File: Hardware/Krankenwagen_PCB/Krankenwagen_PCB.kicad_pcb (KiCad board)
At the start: 2 copper layers, 292.1 x 139 mm, 0 parts

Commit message: Basic PCB completed, added logos to silkscreen
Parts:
- added G***: LOGO, Combat_Robotics:Logo, B.Cu at (134.7, 78.9)
- added G***: LOGO, Combat_Robotics:Krankenwagen_Logo, B.Cu at (173.1, 126.7)
- added H1: 3.5mm Plated Holes, Combat_Robotics:Solder Holes MAMBA X Power, F.Cu at (148.6, 93.6)
- added H4: 2.8mm Plated Holes, Solder_Holes:2.8mm Solder Hole x3, F.Cu at (156.0, 71.9)
- added H7: 2.8mm Plated Holes, Solder_Holes:2.8mm Solder Hole x3, F.Cu at (181.0, 86.1)
- added J1: XT60-M, XT_Connectors:AMASS_XT60-F_1x02_P7.20mm_Vertical, F.Cu at (80.8, 82.6)
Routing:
- net Net-(H4-Pad1): track 0.00 -> 73.3 mm
- net Net-(H4-Pad2): track 0.00 -> 44.1 mm
- net Net-(H4-Pad3): track 0.00 -> 19.7 mm
- added copper zone on B.Cu, net +12V
- added copper zone on F.Cu, net +12V
- added copper zone on B.Cu, net GND
- added copper zone on F.Cu, net GND
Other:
- board size 292.1 x 139 mm -> 119.8 x 88.6 mm
- board text added: "+12V"
- board text added: "Castle 1410"
- board text added: "GND"
- board text added: "MAMBA X"

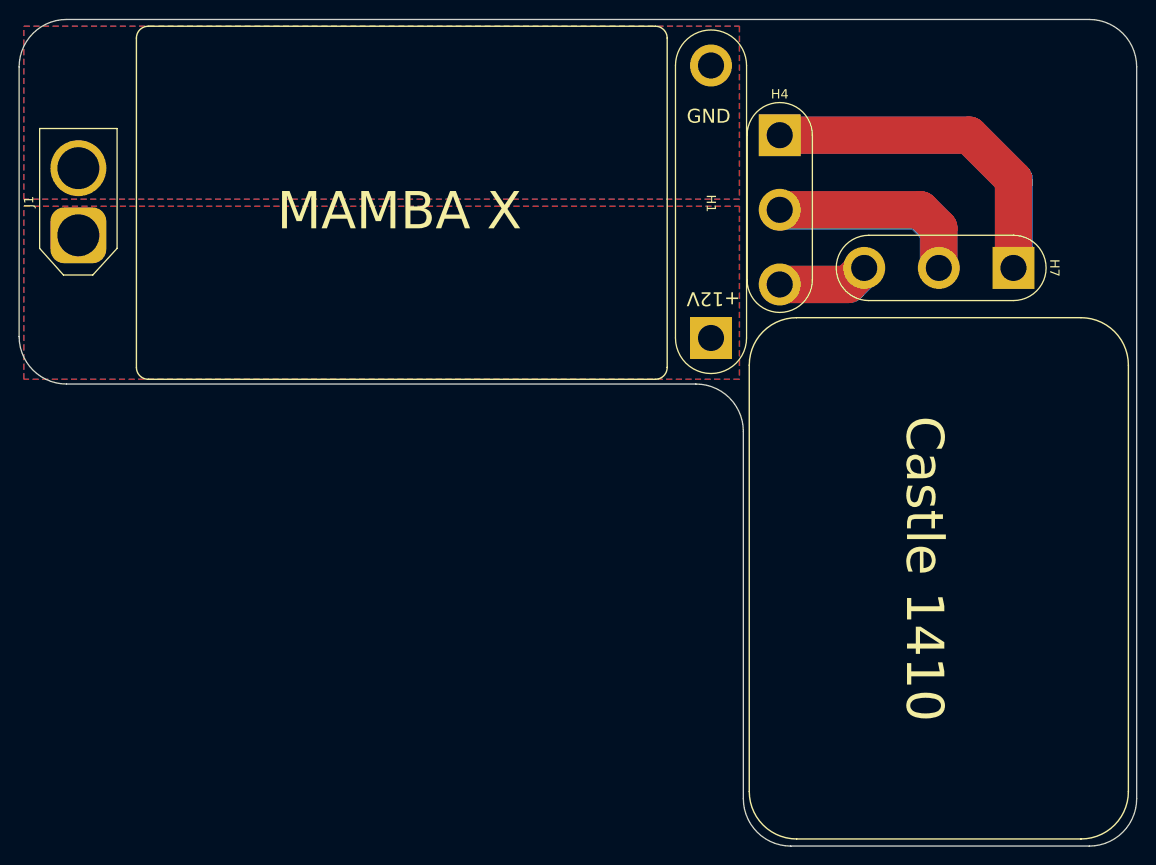
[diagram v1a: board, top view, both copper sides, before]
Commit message: Added mounting holes to PCB and Schematic
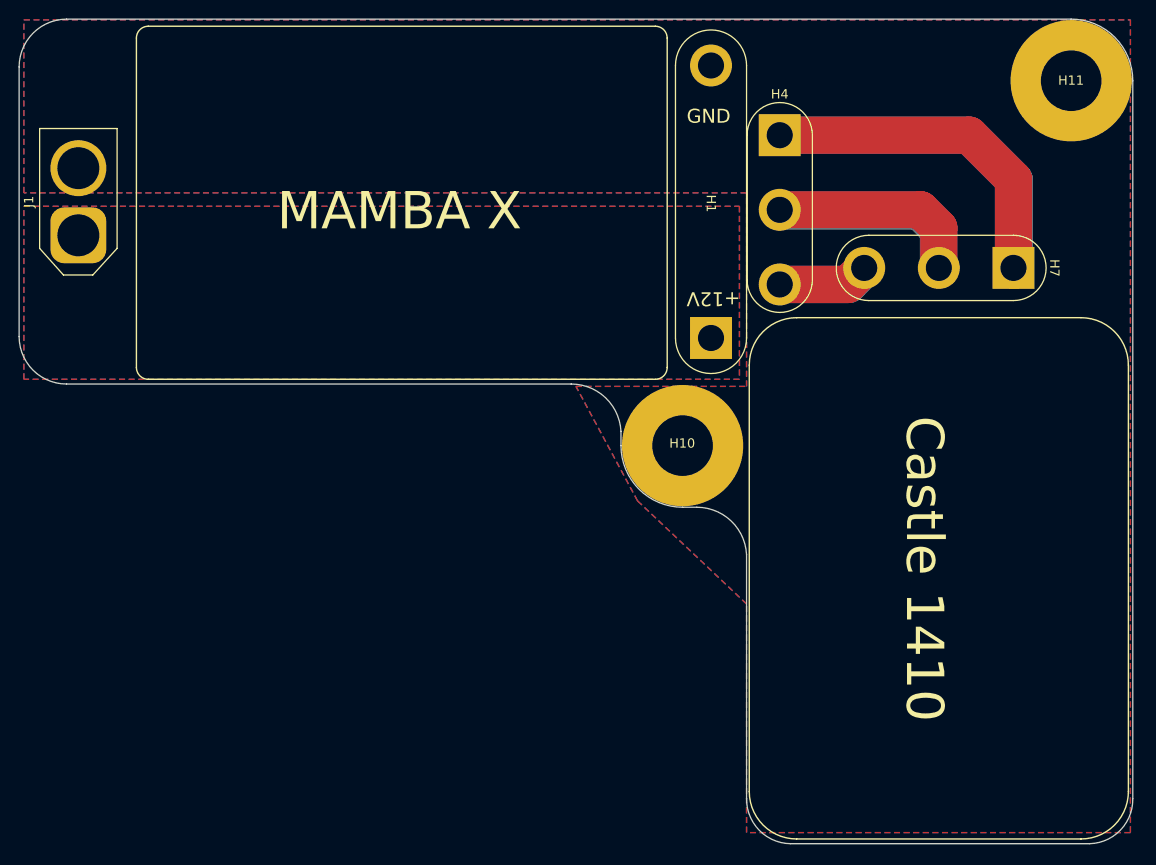
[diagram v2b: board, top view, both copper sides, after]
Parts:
- added H10: MountingHole, MountingHole:MountingHole_6.5mm_Pad, F.Cu at (145.5, 105.2)
- added H11: MountingHole, MountingHole:MountingHole_6.5mm_Pad, F.Cu at (187.2, 66.0)
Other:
- board size 119.8 x 88.6 mm -> 119.4 x 88.4 mm
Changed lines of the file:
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@@
   (net 4 "Net-(H4-Pad2)")
   (net 5 "Net-(H4-Pad3)")
+  (footprint "MountingHole:MountingHole_6.5mm_Pad" (layer "F.Cu")
+    (at 187.198 66.04)
+    (descr "Mounting Hole 6.5mm")
+    (tags "mounting hole 6.5mm")
+    (property "Sheetfile" "Krankenwagen_PCB.kicad_sch")
+    (property "Sheetname" "")
+    (attr exclude_from_pos_files)
+    (fp_text reference "H11" (at -0.018 -0.03) (layer "F.SilkS")
+      (effects (font (size 1 1) (thickness 0.15)))
+    )
+    (fp_text value "MountingHole" (at 0 7.5) (layer "F.Fab")
+      (effects (font (size 1 1) (thickness 0.15)))
+    )
+    (fp_text user "${REFERENCE}" (at 0.3 0) (layer "F.Fab")
+      (effects (font (size 1 1) (thickness 0.15)))
+    )
+    (fp_circle (center 0 0) (end 6.5 0) (layer "Cmts.User") (width 0.15) (fill none))
+    (fp_circle (center 0 0) (end 6.75 0) (layer "F.CrtYd") (width 0.05) (fill none))
+    (pad "1" thru_hole circle (at 0 0) (size 13 13) (drill 6.5) (layers *.Cu *.Mask)
+      (net 2 "GND") (pintype "input"))
+  )
   (footprint "Solder_Holes:2.8mm Solder Hole x3" (layer "F.Cu")
     (at 155.956 71.879)
@@
       (net 5 "Net-(H4-Pad3)") (pintype "input"))
   )
+  (footprint "MountingHole:MountingHole_6.5mm_Pad" (layer "F.Cu")
+    (at 145.542 105.156)
+    (descr "Mounting Hole 6.5mm")
+    (tags "mounting hole 6.5mm")
+    (property "Sheetfile" "Krankenwagen_PCB.kicad_sch")
+    (property "Sheetname" "")
+    (attr exclude_from_pos_files)
+    (fp_text reference "H10" (at -0.042 -0.246) (layer "F.SilkS")
+      (effects (font (size 1 1) (thickness 0.15)))
+    )
+    (fp_text value "MountingHole" (at 0 7.5) (layer "F.Fab")
+      (effects (font (size 1 1) (thickness 0.15)))
+    )
+    (fp_text user "${REFERENCE}" (at 0.3 0) (layer "F.Fab")
+      (effects (font (size 1 1) (thickness 0.15)))
+    )
+    (fp_circle (center 0 0) (end 6.5 0) (layer "Cmts.User") (width 0.15) (fill none))
+    (fp_circle (center 0 0) (end 6.75 0) (layer "F.CrtYd") (width 0.05) (fill none))
+    (pad "1" thru_hole circle (at 0 0) (size 13 13) (drill 6.5) (layers *.Cu *.Mask)
+      (net 2 "GND") (pintype "input"))
+  )
   (footprint "Combat_Robotics:Logo" (layer "B.Cu")
     (at 134.652363 78.938599)
@@
   (gr_line (start 143.891 61.467999) (end 143.891 96.773999) (layer "F.SilkS") (width 0.15))
   (gr_arc (start 142.620999 60.197998) (mid 143.519025 60.569973) (end 143.891 61.467999) (layer "F.SilkS") (width 0.15))
-  (gr_arc (start 189.139102 59.472101) (mid 192.731204 60.959999) (end 194.219102 64.552101) (layer "Edge.Cuts") (width 0.1))
-  (gr_arc (start 194.219101 143.001998) (mid 192.731204 146.594101) (end 189.139101 148.081998) (layer "Edge.Cuts") (width 0.1))
-  (gr_line (start 189.139101 148.081998) (end 157.135101 148.081999) (layer "Edge.Cuts") (width 0.1))
+  (gr_line (start 145.542 111.76) (end 147.066 111.759999) (layer "Edge.Cuts") (width 0.1))
+  (gr_arc (start 193.802 143.001998) (mid 192.470048 146.380717) (end 189.139101 147.828) (layer "Edge.Cuts") (width 0.1))
+  (gr_line (start 189.139101 147.828) (end 157.135101 147.828001) (layer "Edge.Cuts") (width 0.1))
   (gr_arc (start 79.502 98.552) (mid 75.909896 97.064103) (end 74.422001 93.471999) (layer "Edge.Cuts") (width 0.1))
-  (gr_arc (start 74.422001 64.552101) (mid 75.909899 60.959999) (end 79.502001 59.472101) (layer "Edge.Cuts") (width 0.1))
-  (gr_line (start 79.502001 59.472101) (end 189.139102 59.472101) (layer "Edge.Cuts") (width 0.1))
+  (gr_arc (start 74.422001 64.552101) (mid 75.907723 60.947212) (end 79.502 59.436) (layer "Edge.Cuts") (width 0.1))
+  (gr_line (start 79.502 59.436) (end 187.198 59.436) (layer "Edge.Cuts") (width 0.1))
   (gr_line (start 74.422001 93.471999) (end 74.422001 64.552101) (layer "Edge.Cuts") (width 0.1))
-  (gr_line (start 152.055101 143.001999) (end 152.055101 103.631999) (layer "Edge.Cuts") (width 0.1))
-  (gr_arc (start 157.135101 148.081999) (mid 153.542998 146.594102) (end 152.055101 143.001999) (layer "Edge.Cuts") (width 0.1))
-  (gr_line (start 194.219102 64.552101) (end 194.219101 143.001998) (layer "Edge.Cuts") (width 0.1))
-  (gr_line (start 79.502 98.552) (end 146.975101 98.551999) (layer "Edge.Cuts") (width 0.1))
-  (gr_arc (start 146.975101 98.551999) (mid 150.567204 100.039896) (end 152.055101 103.631999) (layer "Edge.Cuts") (width 0.1))
+  (gr_arc (start 133.604 98.552) (mid 137.287 100.025199) (end 138.938 103.631999) (layer "Edge.Cuts") (width 0.1))
+  (gr_line (start 152.4 116.839998) (end 152.4 143.001999) (layer "Edge.Cuts") (width 0.1))
+  (gr_arc (start 145.542 111.76) (mid 140.872267 109.825733) (end 138.938 105.156) (layer "Edge.Cuts") (width 0.1))
+  (gr_line (start 138.938 105.156) (end 138.938 103.631999) (layer "Edge.Cuts") (width 0.1))
+  (gr_arc (start 157.135101 147.828001) (mid 153.768053 146.395672) (end 152.4 143.001999) (layer "Edge.Cuts") (width 0.1))
+  (gr_line (start 193.802 66.04) (end 193.802 143.001998) (layer "Edge.Cuts") (width 0.1))
+  (gr_arc (start 147.066 111.759999) (mid 150.749 113.233198) (end 152.4 116.839998) (layer "Edge.Cuts") (width 0.1))
+  (gr_arc (start 187.198 59.436) (mid 191.867733 61.370267) (end 193.802 66.04) (layer "Edge.Cuts") (width 0.1))
+  (gr_line (start 79.502 98.552) (end 133.604 98.552) (layer "Edge.Cuts") (width 0.1))
   (gr_text "GND" (at 148.336 69.85) (layer "F.SilkS")
     (effects (font (size 1.5 1.5) (thickness 0.3)))
@@
   (segment (start 163.327 87.879) (end 165.1 86.106) (width 4) (layer "B.Cu") (net 5))
   (zone (net 1) (net_name "+12V") (layers F&B.Cu) (hatch edge 0.508)
-    (connect_pads yes (clearance 0.508))
+    (connect_pads yes (clearance 0.762))
     (min_thickness 0.254) (filled_areas_thickness no)
     (fill yes (thermal_gap 0.508) (thermal_bridge_width 0.508))
@@
   )
   (zone (net 2) (net_name "GND") (layers F&B.Cu) (hatch edge 0.508)
-    (connect_pads yes (clearance 0.508))
+    (connect_pads yes (clearance 0.762))
     (min_thickness 0.254) (filled_areas_thickness no)
     (fill yes (thermal_gap 0.508) (thermal_bridge_width 0.508))
     (polygon
       (pts
-        (xy 151.638 78.74)
-        (xy 74.93 78.74)
-        (xy 74.93 60.198)
-        (xy 151.638 60.198)
+        (xy 193.548 146.638)
+        (xy 152.4 146.638)
+        (xy 152.4 122.127)
+        (xy 140.716 111.078)
+        (xy 134.112 98.806)
+        (xy 152.4 98.806)
+        (xy 152.4 78.058)
+        (xy 74.93 78.058)
+        (xy 74.93 59.516)
+        (xy 193.548 59.516)
       )
     )

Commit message: Generated step file of PCB
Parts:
- J1: value XT60-M -> XT60-F
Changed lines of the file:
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@@
     )
     (pad_to_mask_clearance 0)
+    (aux_axis_origin 74.422 59.436)
+    (grid_origin 74.422 59.436)
     (pcbplotparams
       (layerselection 0x00010fc_ffffffff)
@@
       (effects (font (size 1 1) (thickness 0.15)))
     )
-    (fp_text value "XT60-M" (at 3.6 5.4 90) (layer "F.Fab")
+    (fp_text value "XT60-F" (at 3.6 5.4 90) (layer "F.Fab")
       (effects (font (size 1 1) (thickness 0.15)))
     )
@@
     (pad "3" thru_hole circle (at 0 16 270) (size 4.5 4.5) (drill 2.8) (layers *.Cu *.Mask)
       (net 5 "Net-(H4-Pad3)") (pintype "input"))
+    (model "${KIPRJMOD}/LIBRARIES/Castle_Neu_1410_Motor.step"
+      (offset (xyz 33.02 -7.62 18.415))
+      (scale (xyz 1 1 1))
+      (rotate (xyz 0 0 0))
+    )
   )
   (footprint "MountingHole:MountingHole_6.5mm_Pad" (layer "F.Cu")
